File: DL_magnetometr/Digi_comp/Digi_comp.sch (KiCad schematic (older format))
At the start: 46 parts, among them J1 USB_B_Micro, U1 AP7331-WG-7, U2 74AHCT1G125, U3 JST-PHR-2, U4 AZ4558CM, U5 AZ4558CM, U6 AP7331-WG-7, U7 NUP2202, U8 HC-06

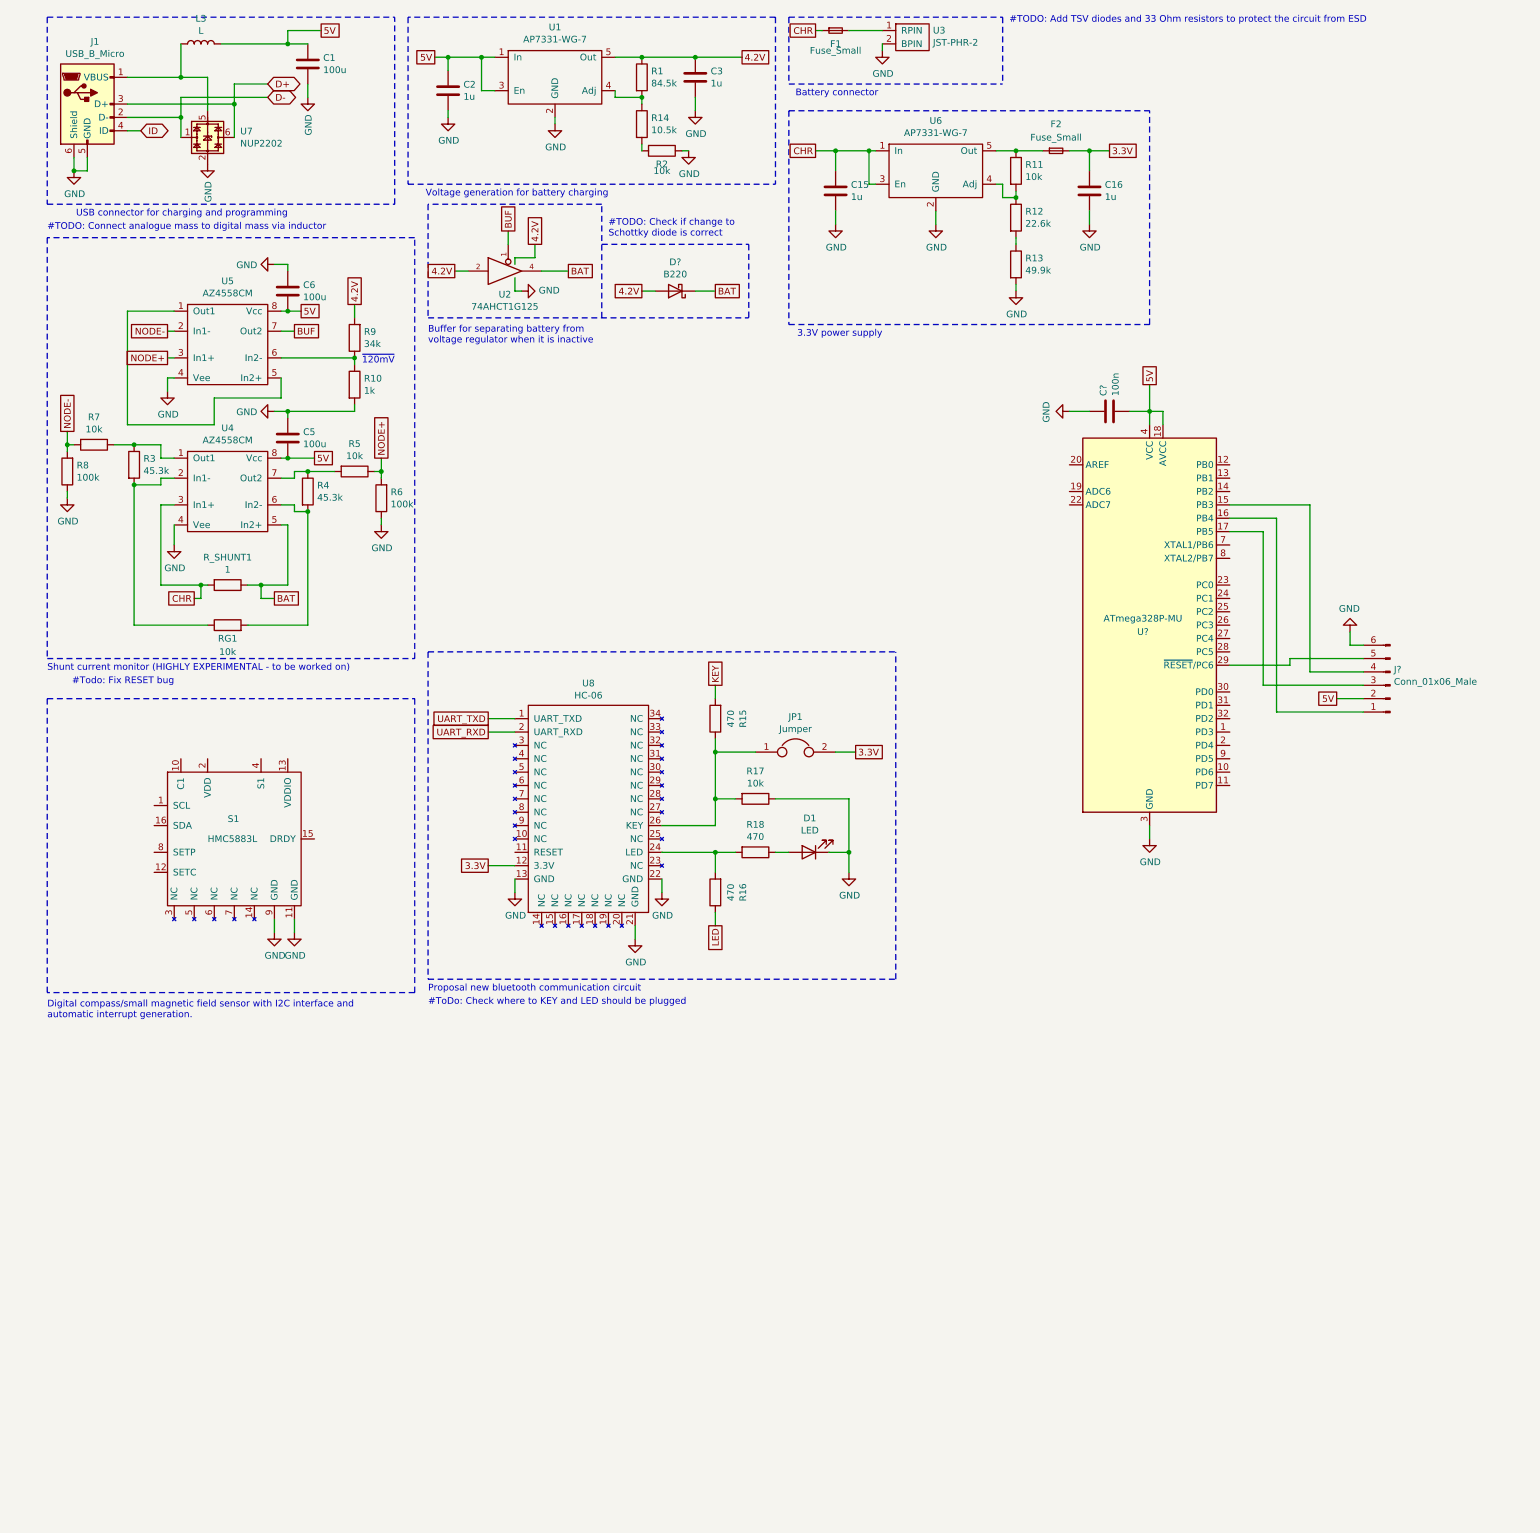
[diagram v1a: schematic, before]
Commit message: Added connections to sensor.
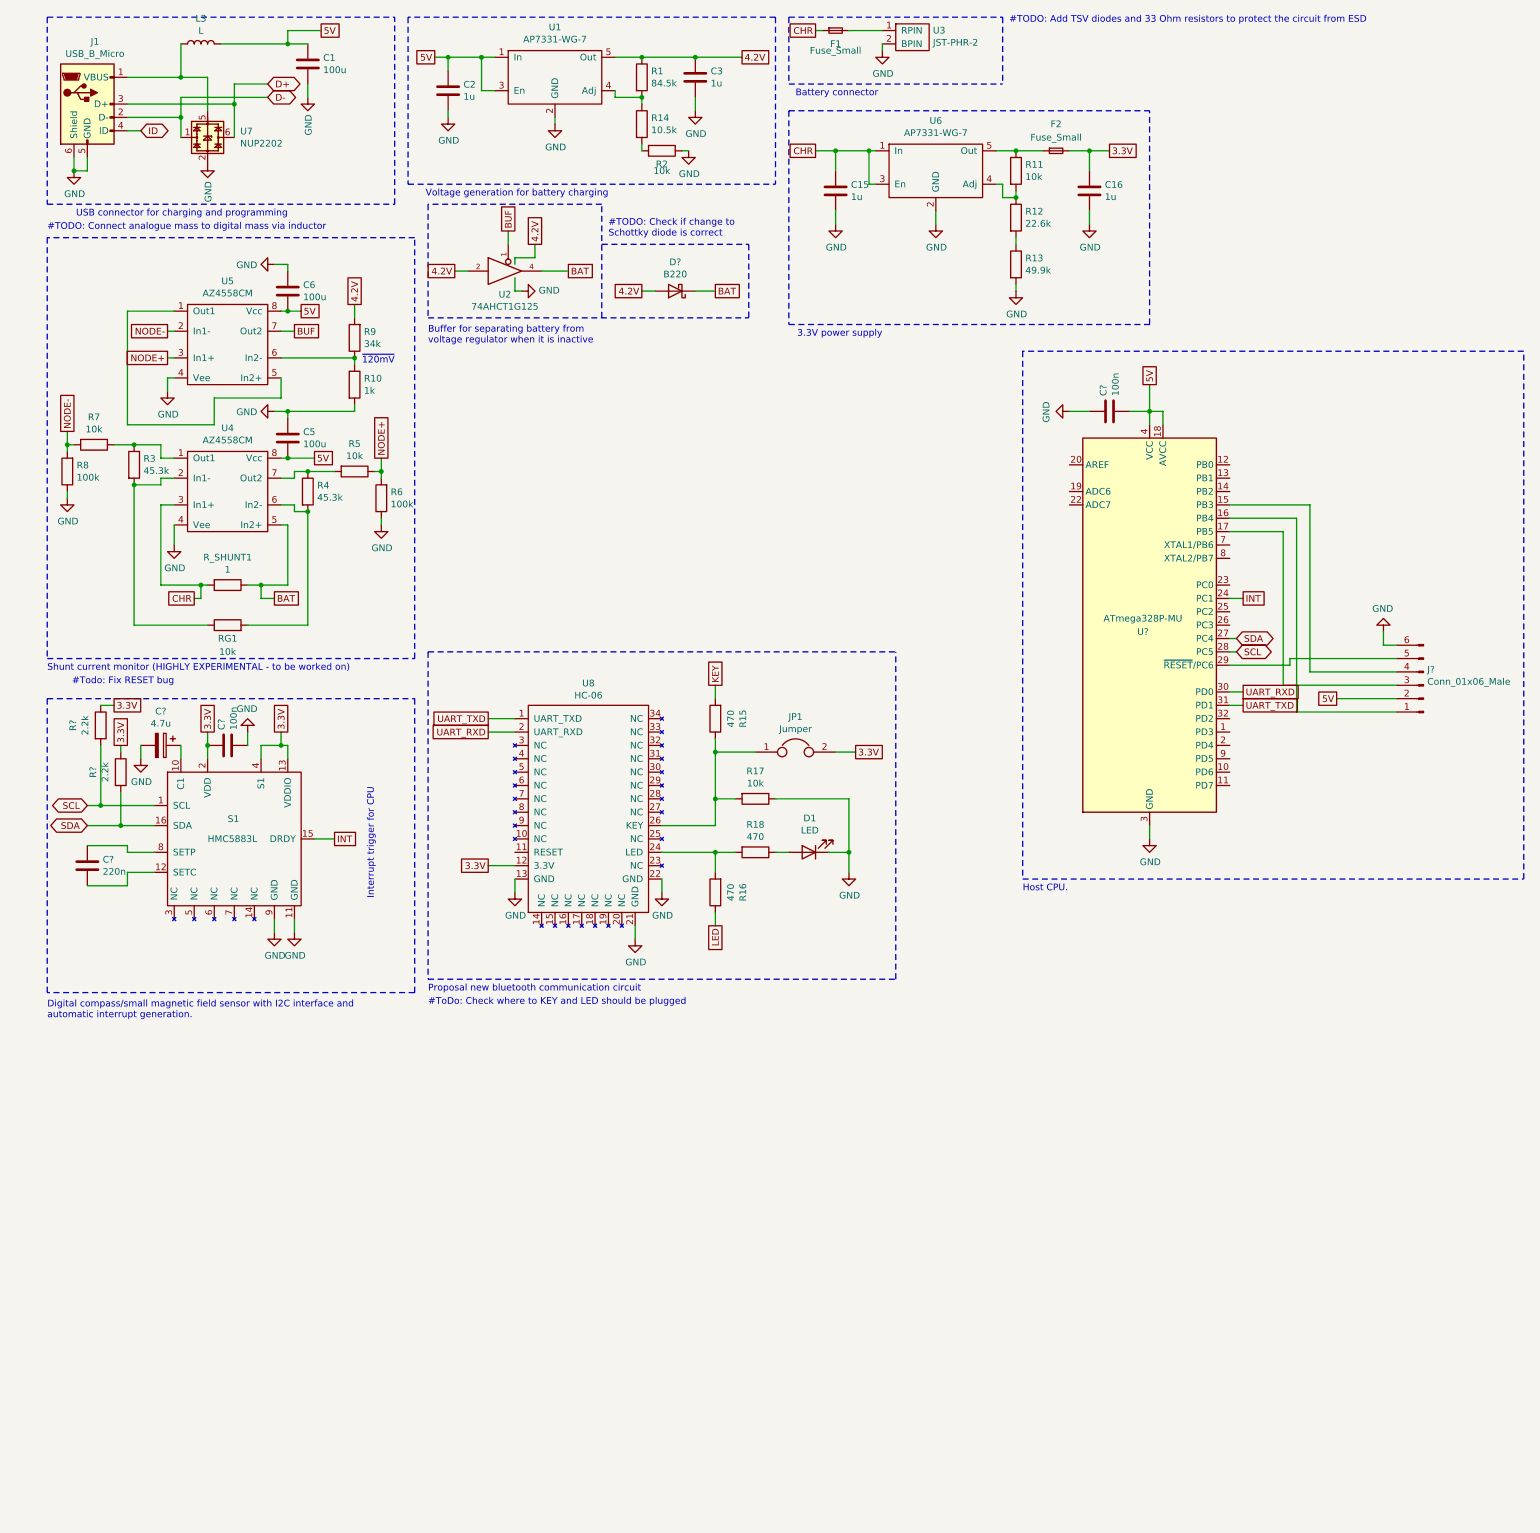
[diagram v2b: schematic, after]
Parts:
- added C?: 220n, symbol Device:C
- added C?: 100n, symbol Device:C
- added C?: 4.7u, symbol Device:CP
- added R? (x2): 2.2k, symbol Device:R
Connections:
- net 3.3V: now also S1.13 (VDDIO), S1.2 (VDD), S1.4 (S1), C?.1, R?.1, R?.1
- net GND: now also C?.2, C?.2
- net UART_RXD: now also U?.30 (PD0)
- net UART_TXD: now also U?.31 (PD1)
- net SCL: now reaches S1.1 (SCL)
- net SCL: now also U?.28 (PC5), R?.2
- net at S1.10 (C1): now also C?.1
- net at S1.12 (SETC): now also C?.2
- net INT: now reaches S1.15 (DRDY)
- net INT: now also U?.24 (PC1)
- net SDA: now reaches S1.16 (SDA)
- net SDA: now also U?.27 (PC4), R?.2
- net at S1.8 (SETP): now also C?.1
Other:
- note added: "Host CPU."
- note added: "Interrupt trigger for CPU"
- moved on the sheet: J?
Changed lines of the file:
@@
 L Connector:Conn_01x06_Male J?
 U 1 1 60070624
-P 10550 5550
-F 0 "J?" H 10522 5432 50  0000 R CNN
-F 1 "Conn_01x06_Male" H 10522 5523 50  0000 R CNN
-F 2 "" H 10550 5550 50  0001 C CNN
-F 3 "~" H 10550 5550 50  0001 C CNN
-	1    10550 5550
+P 10800 5550
+F 0 "J?" H 10772 5432 50  0000 R CNN
+F 1 "Conn_01x06_Male" H 10772 5523 50  0000 R CNN
+F 2 "" H 10800 5550 50  0001 C CNN
+F 3 "~" H 10800 5550 50  0001 C CNN
+	1    10800 5550
 	-1   0    0    1
 $EndComp
@@
 L power:GND #PWR?
 U 1 1 60072062
-P 10250 5150
-F 0 "#PWR?" H 10250 4900 50  0001 C CNN
-F 1 "GND" H 10255 4977 50  0000 C CNN
-F 2 "" H 10250 5150 50  0001 C CNN
-F 3 "" H 10250 5150 50  0001 C CNN
-	1    10250 5150
+P 10500 5150
+F 0 "#PWR?" H 10500 4900 50  0001 C CNN
+F 1 "GND" H 10505 4977 50  0000 C CNN
+F 2 "" H 10500 5150 50  0001 C CNN
+F 3 "" H 10500 5150 50  0001 C CNN
+	1    10500 5150
 	-1   0    0    1
 $EndComp
 Wire Wire Line
-	10350 5250 10250 5250
-Wire Wire Line
-	10250 5250 10250 5150
-Wire Wire Line
-	10350 5350 9800 5350
+	10600 5250 10500 5250
+Wire Wire Line
+	10500 5250 10500 5150
 Wire Wire Line
 	9800 5350 9800 5400
@@
 5V
 Wire Wire Line
-	10350 5650 10150 5650
-Wire Wire Line
-	10350 5750 9700 5750
-Wire Wire Line
-	9700 5750 9700 4300
-Wire Wire Line
-	9700 4300 9350 4300
-Wire Wire Line
-	10350 5450 9950 5450
-Wire Wire Line
 	9950 5450 9950 4200
 Wire Wire Line
 	9950 4200 9350 4200
-Wire Wire Line
-	10350 5550 9600 5550
-Wire Wire Line
-	9600 5550 9600 4400
-Wire Wire Line
-	9600 4400 9350 4400
+Text GLabel 9450 4900 2    50   UnSpc ~ 0
+INT
+Wire Wire Line
+	9450 4900 9350 4900
+Text GLabel 2650 6700 2    50   UnSpc ~ 0
+INT
+Wire Wire Line
+	2650 6700 2500 6700
+Text Notes 2950 7150 1    50   ~ 0
+Interrupt trigger for CPU
+Text GLabel 800  6450 0    50   BiDi ~ 0
+SCL
+Text GLabel 800  6600 0    50   BiDi ~ 0
+SDA
+Text GLabel 9400 5300 2    50   BiDi ~ 0
+SCL
+Wire Wire Line
+	9400 5300 9350 5300
+Wire Wire Line
+	9750 4400 9750 5550
+Wire Wire Line
+	9350 4400 9750 4400
+Wire Wire Line
+	9850 4300 9850 5750
+Wire Wire Line
+	9850 5750 10600 5750
+Wire Wire Line
+	9350 4300 9850 4300
+Wire Wire Line
+	10150 5650 10600 5650
+Wire Wire Line
+	9750 5550 10600 5550
+Wire Wire Line
+	9950 5450 10600 5450
+Wire Wire Line
+	9800 5350 10600 5350
+Text GLabel 9400 5200 2    50   BiDi ~ 0
+SDA
+Wire Wire Line
+	9400 5200 9350 5200
+Text GLabel 9450 5700 2    50   UnSpc ~ 0
+UART_TXD
+Wire Wire Line
+	9450 5700 9350 5700
+Text GLabel 9450 5600 2    50   UnSpc ~ 0
+UART_RXD
+Wire Wire Line
+	9450 5600 9350 5600
+$Comp
+L Device:C C?
+U 1 1 6008913F
+P 800 6900
+F 0 "C?" H 915 6946 50  0000 L CNN
+F 1 "220n" H 915 6855 50  0000 L CNN
+F 2 "" H 838 6750 50  0001 C CNN
+F 3 "~" H 800 6900 50  0001 C CNN
+	1    800  6900
+	1    0    0    -1
+$EndComp
+Wire Wire Line
+	800  6750 1100 6750
+Wire Wire Line
+	1100 6750 1100 6800
+Wire Wire Line
+	1100 6800 1300 6800
+Wire Wire Line
+	800  7050 1100 7050
+Wire Wire Line
+	1100 7050 1100 6950
+Wire Wire Line
+	1100 6950 1300 6950
+Text GLabel 1700 5900 1    50   UnSpc ~ 0
+3.3V
+$Comp
+L Device:C C?
+U 1 1 6009E292
+P 1850 6000
+F 0 "C?" H 1965 6046 50  0000 L CNN
+F 1 "100n" H 1965 5955 50  0000 L CNN
+F 2 "" H 1888 5850 50  0001 C CNN
+F 3 "~" H 1850 6000 50  0001 C CNN
+	1    1850 6000
+	0    -1   -1   0
+$EndComp
+Wire Wire Line
+	1700 6100 1700 6000
+Wire Wire Line
+	1700 5900 1700 6000
+Connection ~ 1700 6000
+$Comp
+L power:GND #PWR?
+U 1 1 600B414B
+P 2000 5900
+F 0 "#PWR?" H 2000 5650 50  0001 C CNN
+F 1 "GND" H 2005 5727 50  0000 C CNN
+F 2 "" H 2000 5900 50  0001 C CNN
+F 3 "" H 2000 5900 50  0001 C CNN
+	1    2000 5900
+	-1   0    0    1
+$EndComp
+Wire Wire Line
+	2000 6000 2000 5900
+Wire Wire Line
+	1500 6100 1500 6000
+$Comp
+L power:GND #PWR?
+U 1 1 600CAB00
+P 1200 6100
+F 0 "#PWR?" H 1200 5850 50  0001 C CNN
+F 1 "GND" H 1205 5927 50  0000 C CNN
+F 2 "" H 1200 6100 50  0001 C CNN
+F 3 "" H 1200 6100 50  0001 C CNN
+	1    1200 6100
+	1    0    0    -1
+$EndComp
+Wire Wire Line
+	1200 6100 1200 6000
+$Comp
+L Device:CP C?
+U 1 1 600D6749
+P 1350 6000
+F 0 "C?" V 1095 6000 50  0000 C CNN
+F 1 "4.7u" V 1186 6000 50  0000 C CNN
+F 2 "" H 1388 5850 50  0001 C CNN
+F 3 "~" H 1350 6000 50  0001 C CNN
+	1    1350 6000
+	0    1    1    0
+$EndComp
+$Comp
+L Device:R R?
+U 1 1 600D7AA2
+P 900 5850
+F 0 "R?" V 693 5850 50  0000 C CNN
+F 1 "2.2k" V 784 5850 50  0000 C CNN
+F 2 "" V 830 5850 50  0001 C CNN
+F 3 "~" H 900 5850 50  0001 C CNN
+	1    900  5850
+	1    0    0    -1
+$EndComp
+$Comp
+L Device:R R?
+U 1 1 600D8CF5
+P 1050 6200
+F 0 "R?" V 843 6200 50  0000 C CNN
+F 1 "2.2k" V 934 6200 50  0000 C CNN
+F 2 "" V 980 6200 50  0001 C CNN
+F 3 "~" H 1050 6200 50  0001 C CNN
+	1    1050 6200
+	1    0    0    -1
+$EndComp
+Wire Wire Line
+	1050 6350 1050 6600
+Wire Wire Line
+	1050 6600 1300 6600
+Wire Wire Line
+	1050 6600 800  6600
+Connection ~ 1050 6600
+Wire Wire Line
+	800  6450 900  6450
+Wire Wire Line
+	900  6000 900  6450
+Connection ~ 900  6450
+Wire Wire Line
+	900  6450 1300 6450
+Text GLabel 1050 6000 1    50   UnSpc ~ 0
+3.3V
+Wire Wire Line
+	1050 6050 1050 6000
+Text GLabel 1000 5700 2    50   UnSpc ~ 0
+3.3V
+Wire Wire Line
+	1000 5700 900  5700
+Text GLabel 2250 5900 1    50   UnSpc ~ 0
+3.3V
+Wire Wire Line
+	2250 5900 2250 6000
+Wire Wire Line
+	2250 6000 2100 6000
+Wire Wire Line
+	2100 6000 2100 6100
+Wire Wire Line
+	2250 6000 2300 6000
+Wire Wire Line
+	2300 6000 2300 6100
+Connection ~ 2250 6000
+Wire Notes Line
+	7800 3050 7800 7000
+Wire Notes Line
+	7800 7000 11550 7000
+Wire Notes Line
+	11550 7000 11550 3050
+Wire Notes Line
+	11550 3050 7800 3050
+Text Notes 7800 7100 0    50   ~ 0
+Host CPU.
 $EndSCHEMATC

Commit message: Added more info to documentation
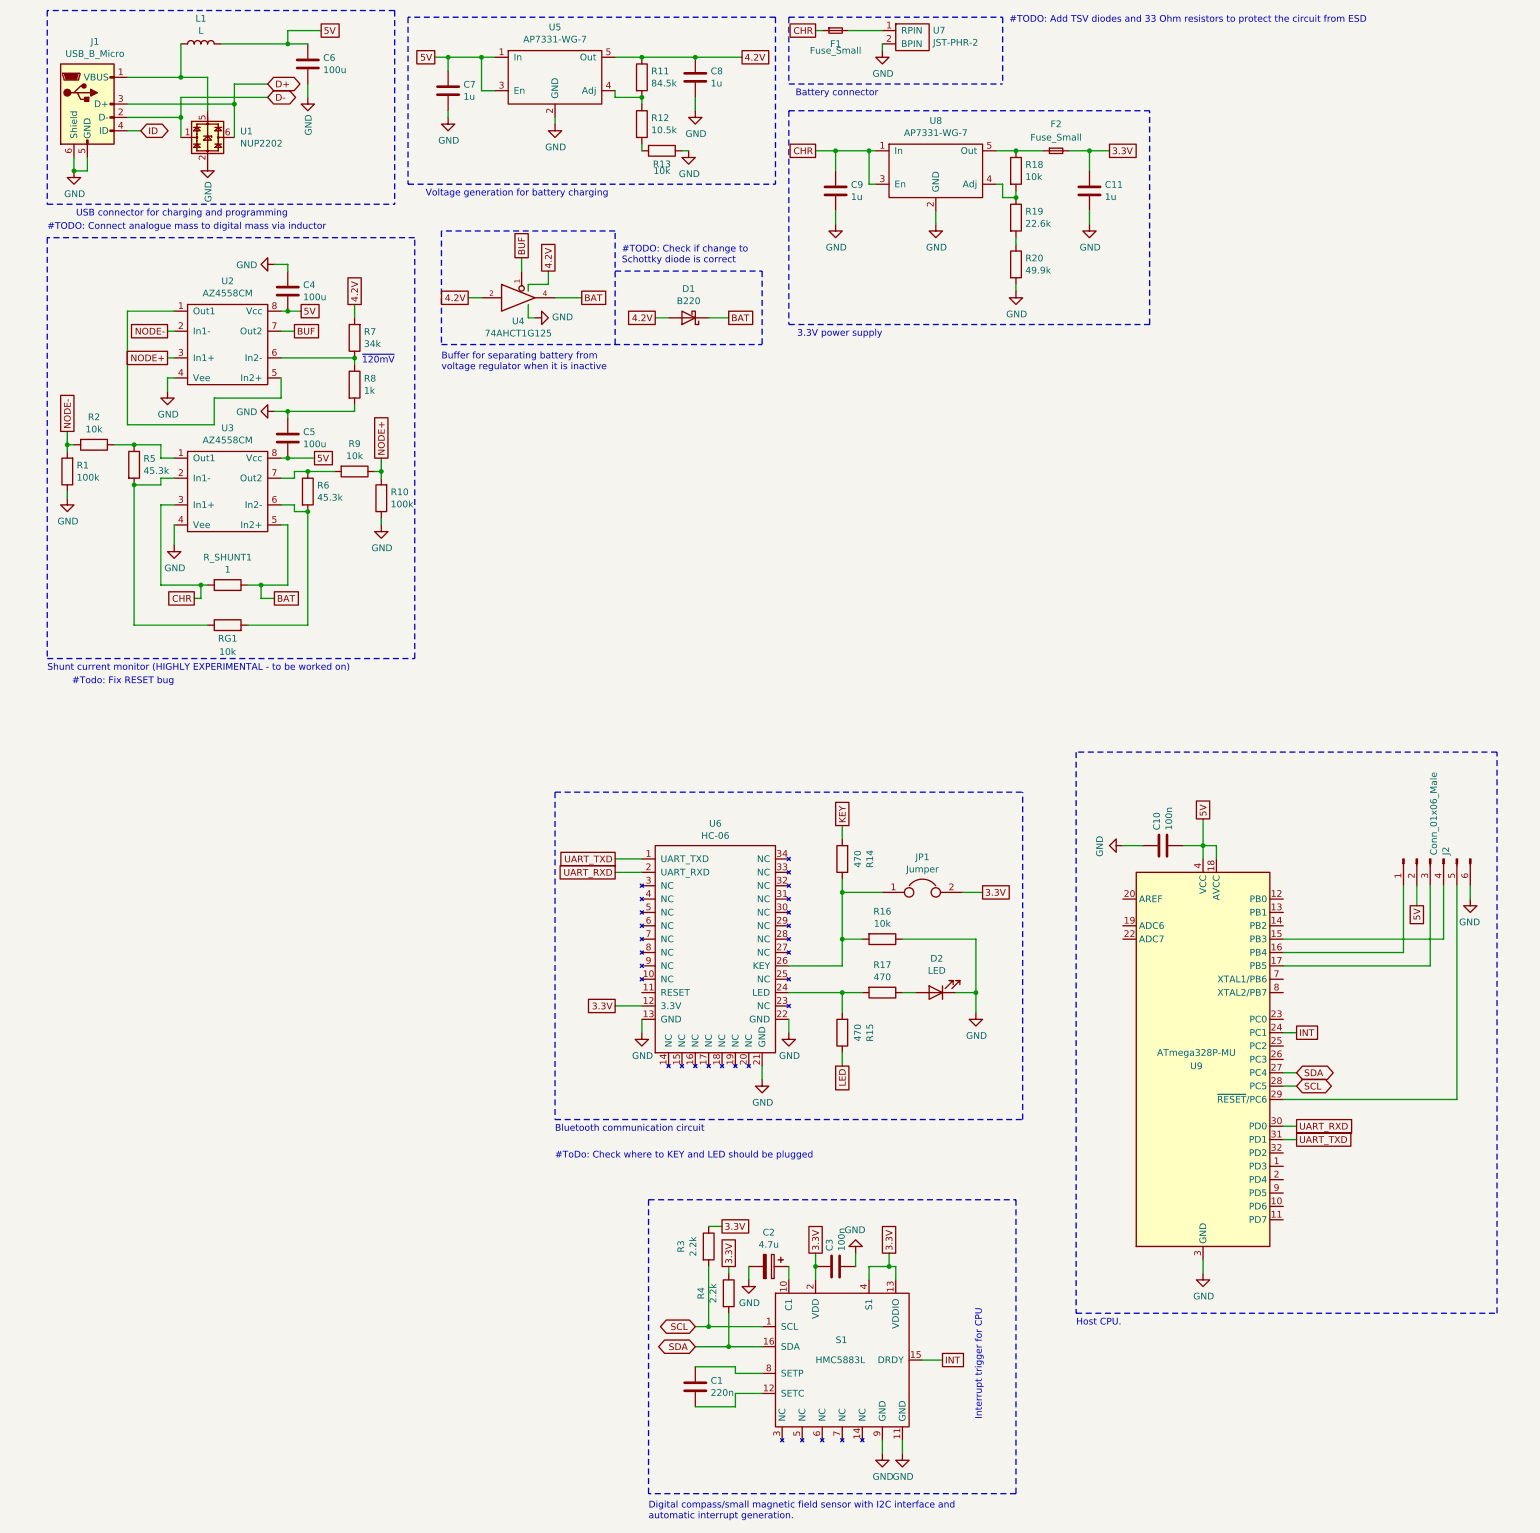
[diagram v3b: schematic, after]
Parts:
- gave numbers to parts that had none: 9
- renumbered C16 to C11, C6 to C4, C1 to C6, C2 to C7, C3 to C8, C15 to C9, D1 to D2, L3 to L1, R8 to R1, R6 to R10, R1 to R11, R14 to R12, R2 to R13, R15 to R14, R16 to R15, R17 to R16, R18 to R17, R11 to R18, R12 to R19, R7 to R2, R13 to R20, R3 to R5, R4 to R6, R9 to R7, R10 to R8, R5 to R9, U7 to U1, U5 to U2, U4 to U3, U2 to U4, U1 to U5, U8 to U6, U3 to U7, U6 to U8
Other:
- note added: "Bluetooth communication circuit\n"
- note removed: "Proposal new bluetooth communication circuit\n"
- moved on the sheet: C1, C10, C2, C3, D1, D2, J2, JP1, R14, R15, R16, R17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

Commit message: Added some footprints, started layout
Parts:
- C1, C10, C2, C3: footprint (none) -> Capacitor_SMD:C_0805_2012Metric
- D2: footprint (none) -> Diode_SMD:D_0805_2012Metric
- J2: footprint (none) -> Connector_PinHeader_2.54mm:PinHeader_1x06_P2.54mm_Vertical
- JP1: footprint (none) -> Jumper:SolderJumper-3_P1.3mm_Bridged12_Pad1.0x1.5mm
- R14, R15, R16, R17, R18, R19, R20, R3, R4: footprint (none) -> Resistor_SMD:R_0805_2012Metric
- S1: footprint (none) -> Dokumenty:XDCR_HMC5883L-TR
- U5, U8: footprint (none) -> Package_TO_SOT_SMD:TSOT-23-5
- U6: footprint (none) -> Dokumenty:XCVR_BLUETOOTH-SERIAL-HC-06
